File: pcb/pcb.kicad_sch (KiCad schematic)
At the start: 28 parts, among them IC1 TC78H660FTG,EL, J1 Screw_Terminal_01x02, J2 Conn_01x06_Male, J3 Screw_Terminal_01x02, J4 Screw_Terminal_01x02, Q1 Q_PMOS_GSD, U1 ME431

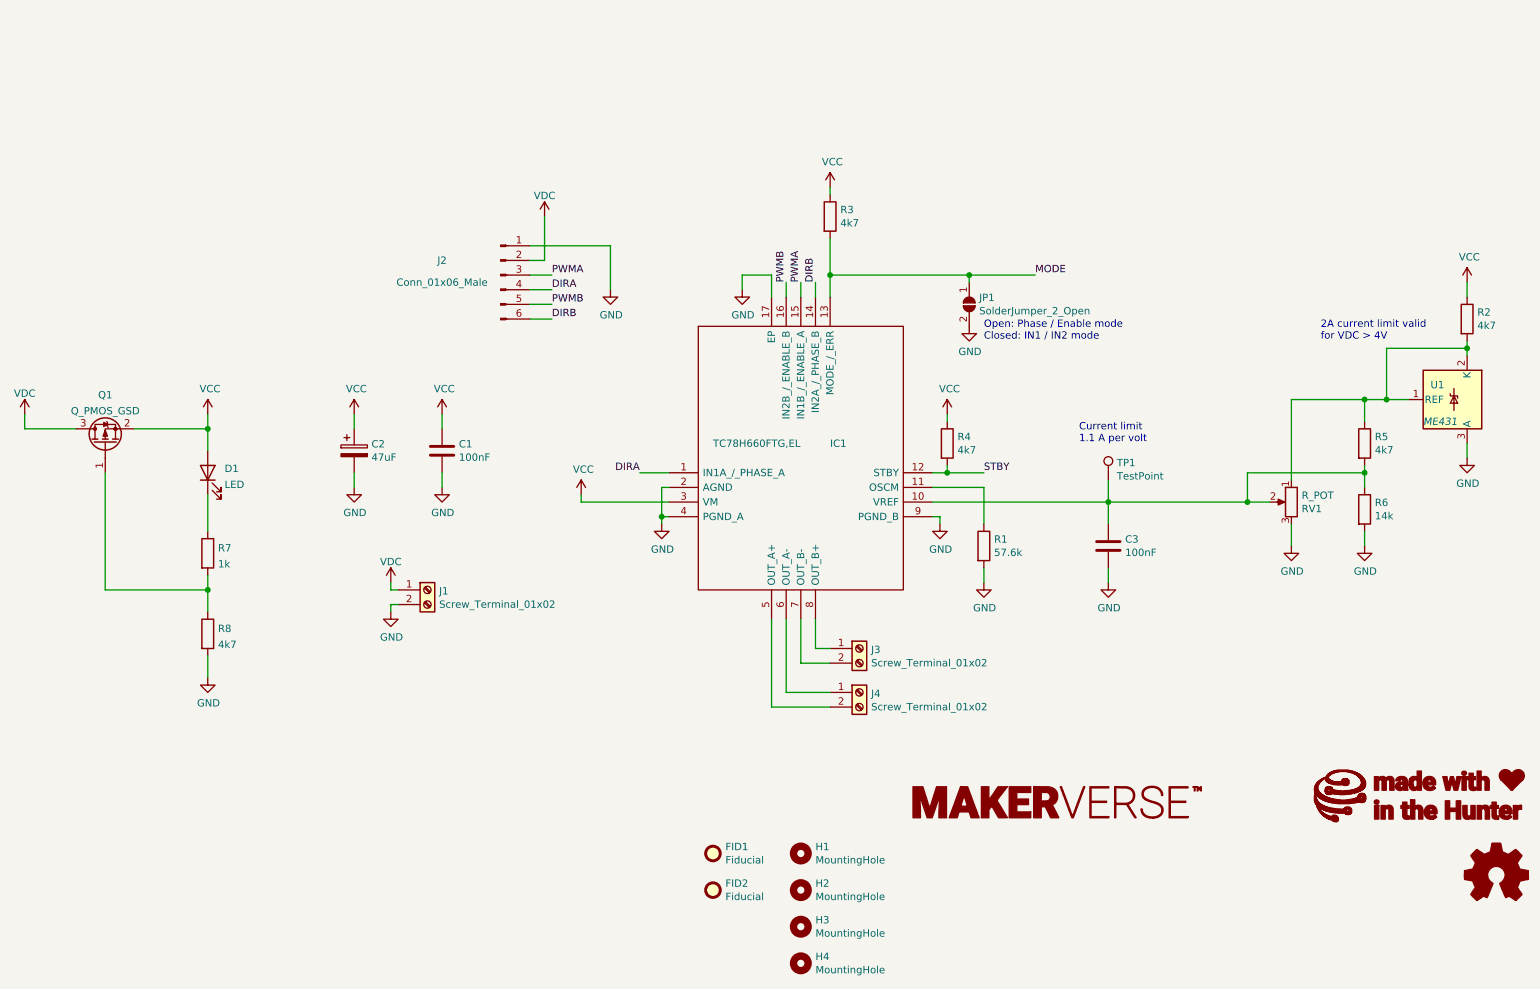
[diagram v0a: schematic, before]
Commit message: v20 update with voltage regulator
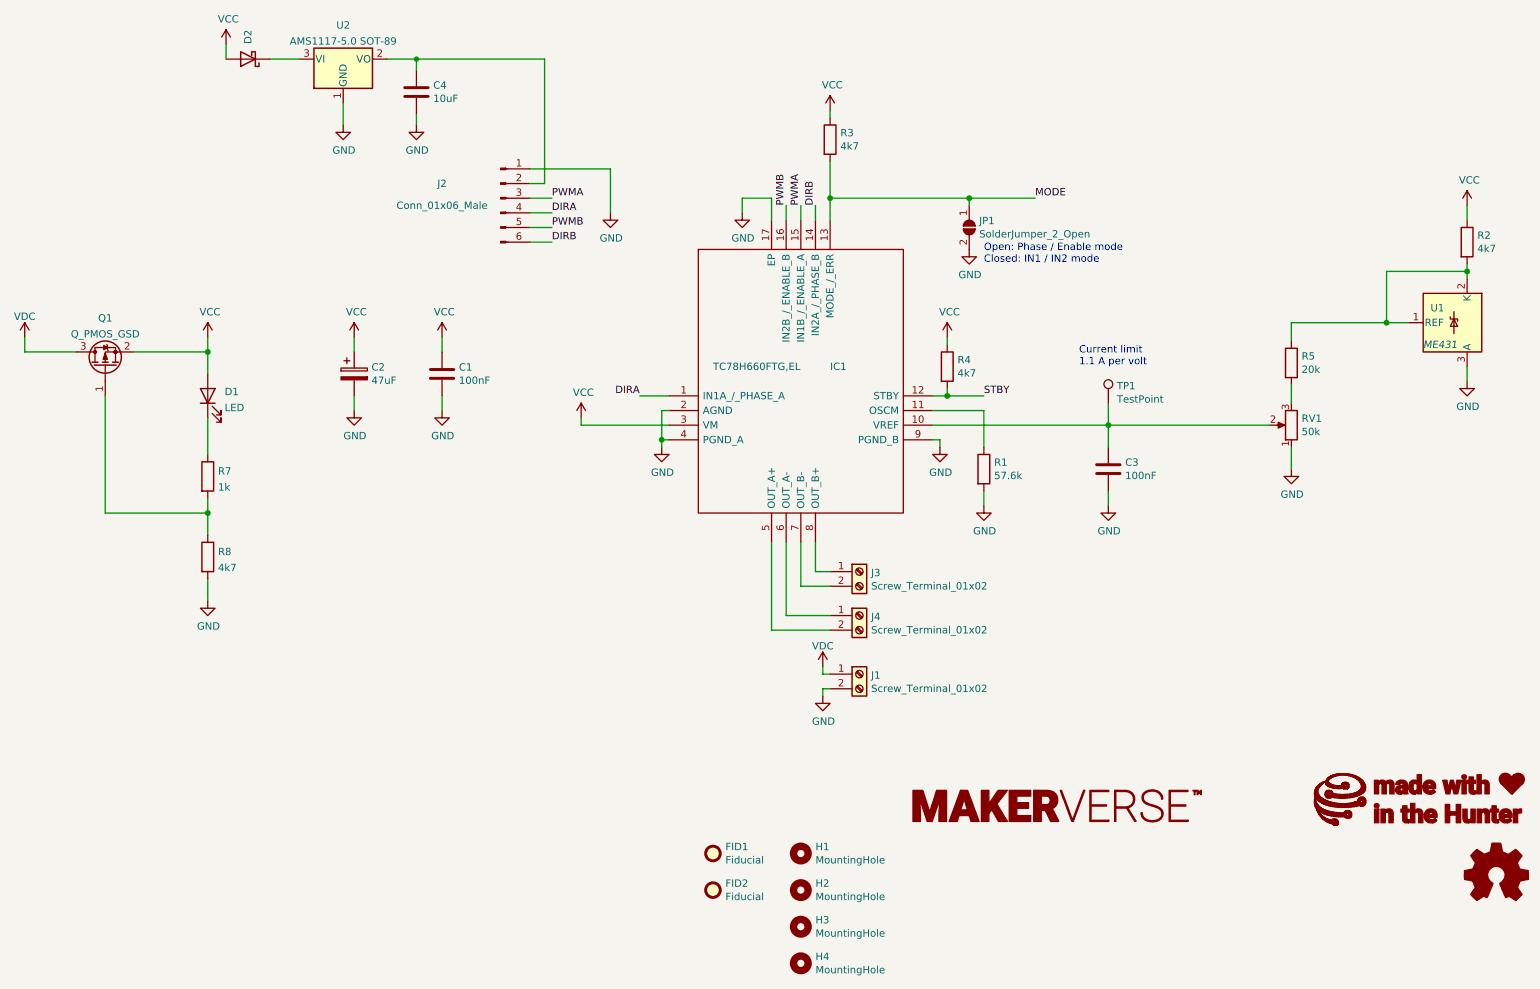
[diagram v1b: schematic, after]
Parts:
- removed R6: 14k, Resistor_SMD:R_0402_1005Metric, symbol Device:R
- added C4: 10uF, Capacitor_SMD:C_0603_1608Metric, symbol Device:C
- added D2: D_Schottky, Diode_SMD:D_SMA, symbol Device:D_Schottky
- added U2: AMS1117-5.0 SOT-89, Package_TO_SOT_SMD:SOT-89-3, symbol Regulator_Linear:AMS1117-5.0
- IC1: footprint lib:QFN50P300X300X90-17N -> Package_DFN_QFN:QFN-16-1EP_3x3mm_P0.5mm_EP1.7x1.7mm_ThermalVias
- R5: value 4k7 -> 20k
- RV1: value R_POT -> 50k; footprint Potentiometer_THT:Potentiometer_Bourns_3296W_Vertical -> lib:smdPot
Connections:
- net GND: now also RV1.1, C4.2, U2.1 (GND); no longer RV1.3
- net VCC: now also D2.2 (A)
- net VDC: no longer J2.2 (Pin_2)
- net at C3.1, IC1.10 (VREF), RV1.2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: no longer R5.2
- net at R2.2, R5.1, U1.1 (REF)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: no longer RV1.1
- new net: R5.2, RV1.3
- new net: C4.1, J2.2 (Pin_2), U2.2 (VO)
- new net: D2.1 (K), U2.3 (VI)
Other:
- note removed: "2A current limit valid for VDC > 4V"
- moved on the sheet: C1, C2, C3, D1, IC1, J1, J2, J3, J4, JP1, Q1, R1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
